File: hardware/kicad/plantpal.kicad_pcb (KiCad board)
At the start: 2 copper layers, 38.4 x 128.5 mm, 117 parts, among them J1 U262-161N-4BVC11, J2 +LIPO, J3 -LIPO, J4 687124182122, Q1 DMG1012UW, Q2 DMG3415U-7, Q3 MMBT3906, Q4 PMV32UP, Q5 DMG1012UW, Q6 AO3407A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

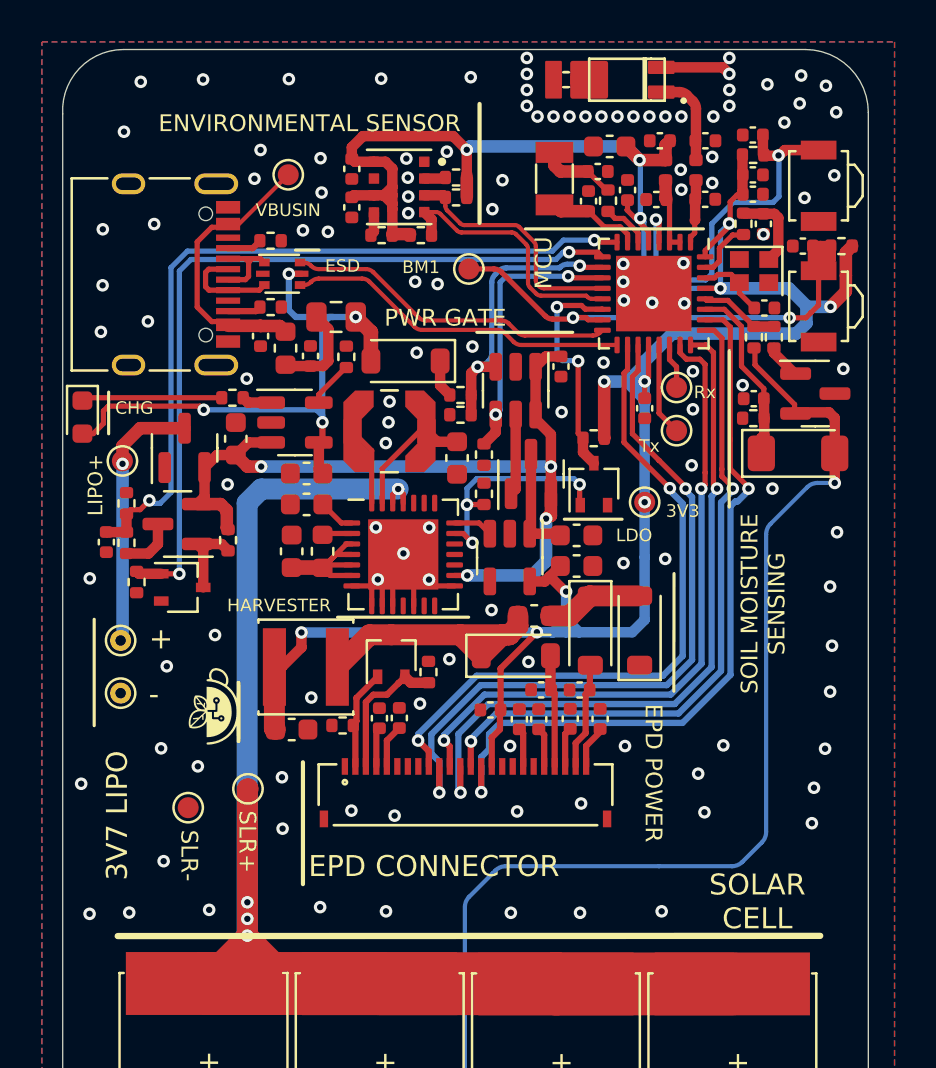
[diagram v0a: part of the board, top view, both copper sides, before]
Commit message: add testpin for chip_enable
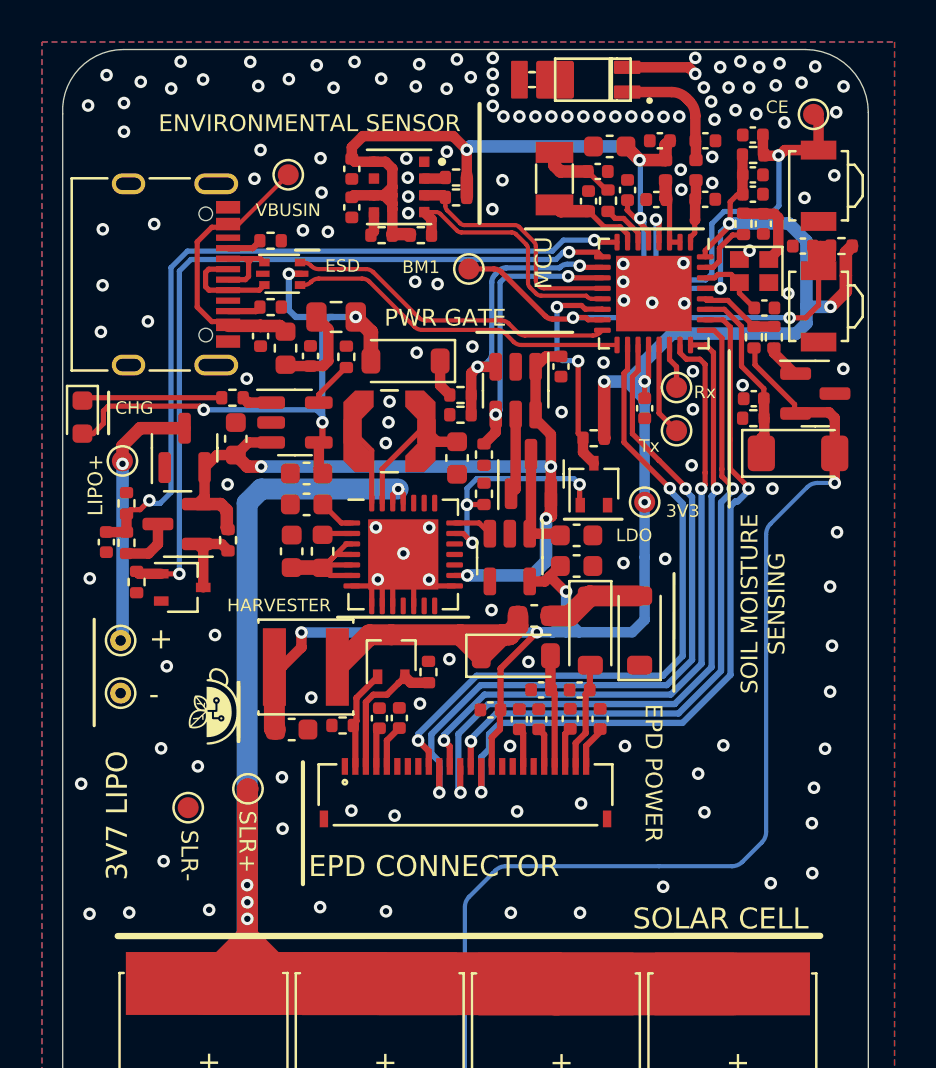
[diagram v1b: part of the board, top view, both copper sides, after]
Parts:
- added TP9: CHIP_EN, TestPoint:TestPoint_Pad_D1.0mm, F.Cu at (126.3, 36.0)
- moved AE1 1.62 mm to (116.0, 34.4)
- moved C12 1.62 mm to (112.8, 34.4)
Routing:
- net +3V3: track 128.0 -> 130.7 mm
- net /Main Controller/CHIP_EN: track 18.4 -> 20.5 mm
- net Net-(AE1-FEED): track 4.52 -> 6.03 mm
- net GND: vias 124 -> 151
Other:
- board text added: "CE"

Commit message: wip
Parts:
- moved TP9 30.3 mm to (124.7, 66.2)
- moved G*** 27.9 mm to (125.0, 70.0), turned to 0 degrees
- moved TP5 12.8 mm to (122.1, 66.7)
- moved C29 1.99 mm to (94.4, 55.8)
- moved R20 1.98 mm to (95.4, 55.8)
- moved Q4 1.86 mm to (97.8, 55.9)
- moved R22 1.83 mm to (100.2, 56.3)
- moved AE1 1.62 mm to (117.6, 34.4)
- moved C12 1.62 mm to (114.5, 34.4)
- moved R23 1.47 mm to (94.9, 57.2), turned to 180 degrees
- moved R21 1.42 mm to (94.9, 54.3), turned to 0 degrees
- moved Q5 0.70 mm to (95.6, 58.9)
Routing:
- net /Main Controller/CHIP_EN: track 20.5 -> 47.6 mm, vias 2 -> 3
- net +3V3: track 130.7 -> 145.6 mm, vias 12 -> 11
- net /Solar Power/SOLAR+: track 70.9 -> 65.5 mm
- net /Main Controller/BATT_MEAS: track 37.1 -> 34.8 mm
- net Net-(AE1-FEED): track 6.03 -> 4.52 mm
- net Net-(Q4-G): track 3.80 -> 5.16 mm
- net /Main Controller/PWR_STATUS: track 11.2 -> 10.1 mm
- net Net-(Q4-D): track 2.64 -> 1.63 mm
- net /Main Controller/BATT_MEAS_EN: track 37.2 -> 36.6 mm
- net +BATT: track 39.1 -> 39.2 mm, vias 4 -> 3
- net Net-(J2-Pin_1): track 12.6 -> 12.8 mm, vias 1 -> 0
- net GND: vias 151 -> 184
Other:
- board text added: "PWR INPUT"

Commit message: wip
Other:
- board text added: "BATT SENSE"

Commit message: wip wake-up button
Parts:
- added Q8: PMV32UP, Package_TO_SOT_SMD:SOT-23, F.Cu at (1.95, 1.73)
- added R27: 5K1, Resistor_SMD:R_0402_1005Metric, F.Cu at (0.95, 4.95)
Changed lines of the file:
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@@
   (net 87 "unconnected-(J4-TSCL-Pad6)")
   (net 88 "unconnected-(J4-TSDA-Pad7)")
+  (net 89 "Net-(Q8-D)")
   (footprint "Capacitor_SMD:C_0402_1005Metric" (layer "F.Cu")
     (at 123.378 39.837)
@@
     (pad "1" thru_hole circle (at 0 0) (size 1 1) (drill 0.5) (layers "*.Cu" "*.Mask")
       (net 43 "Net-(J2-Pin_1)") (pinfunction "Pin_1") (pintype "passive"))
+  )
+  (footprint "Package_TO_SOT_SMD:SOT-23" (layer "F.Cu")
+    (at 1.945 1.725)
+    (descr "SOT, 3 Pin (https://www.jedec.org/system/files/docs/to-236h.pdf variant AB), generated with kicad-footprint-generator ipc_gullwing_generator.py")
+    (tags "SOT TO_SOT_SMD")
+    (property "Distributor" "LCSC")
+    (property "Distributor Link" "https://www.lcsc.com/product-detail/MOSFETs_TECH-PUBLIC-PMV32UP_C2959851.html")
+    (property "Distributor Part Number" "C2959851")
+    (property "Manufacturer" "TECH PUBLIC")
+    (property "Manufacturer Part Number" "PMV32UP")
+    (property "Part Description" "MOSFET P Channel 20V 4A 52mΩ@4.5V")
+    (property "Sheetfile" "power_gate_and_regulator.kicad_sch")
+    (property "Sheetname" "Power Gate and Regulator")
+    (property "ki_description" "P-MOSFET transistor, gate/source/drain")
+    (property "ki_keywords" "transistor PMOS P-MOS P-MOSFET")
+    (attr smd)
+    (fp_text reference "Q8" (at 0 -2.4) (layer "F.SilkS")
+        (effects (font (size 1 1) (thickness 0.15)))
+    )
+    (fp_text value "PMV32UP" (at 0 2.4) (layer "F.Fab")
+        (effects (font (size 1 1) (thickness 0.15)))
+    )
+    (fp_text user "${REFERENCE}" (at 0 0) (layer "F.Fab")
+        (effects (font (size 0.32 0.32) (thickness 0.05)))
+    )
+    (fp_line (start 0 -1.56) (end -1.675 -1.56)
+      (stroke (width 0.12) (type solid)) (layer "F.SilkS"))
+    (fp_line (start 0 -1.56) (end 0.65 -1.56)
+      (stroke (width 0.12) (type solid)) (layer "F.SilkS"))
+    (fp_line (start 0 1.56) (end -0.65 1.56)
+      (stroke (width 0.12) (type solid)) (layer "F.SilkS"))
+    (fp_line (start 0 1.56) (end 0.65 1.56)
+      (stroke (width 0.12) (type solid)) (layer "F.SilkS"))
+    (fp_line (start -1.92 -1.7) (end -1.92 1.7)
+      (stroke (width 0.05) (type solid)) (layer "F.CrtYd"))
+    (fp_line (start -1.92 1.7) (end 1.92 1.7)
+      (stroke (width 0.05) (type solid)) (layer "F.CrtYd"))
+    (fp_line (start 1.92 -1.7) (end -1.92 -1.7)
+      (stroke (width 0.05) (type solid)) (layer "F.CrtYd"))
+    (fp_line (start 1.92 1.7) (end 1.92 -1.7)
+      (stroke (width 0.05) (type solid)) (layer "F.CrtYd"))
+    (fp_line (start -0.65 -1.125) (end -0.325 -1.45)
+      (stroke (width 0.1) (type solid)) (layer "F.Fab"))
+    (fp_line (start -0.65 1.45) (end -0.65 -1.125)
+      (stroke (width 0.1) (type solid)) (layer "F.Fab"))
+    (fp_line (start -0.325 -1.45) (end 0.65 -1.45)
+      (stroke (width 0.1) (type solid)) (layer "F.Fab"))
+    (fp_line (start 0.65 -1.45) (end 0.65 1.45)
+      (stroke (width 0.1) (type solid)) (layer "F.Fab"))
+    (fp_line (start 0.65 1.45) (end -0.65 1.45)
+      (stroke (width 0.1) (type solid)) (layer "F.Fab"))
+    (pad "1" smd roundrect (at -0.9375 -0.95) (size 1.475 0.6) (layers "F.Cu" "F.Paste" "F.Mask") (roundrect_rratio 0.25)
+      (net 11 "/Main Controller/CHIP_EN") (pinfunction "G") (pintype "input"))
+    (pad "2" smd roundrect (at -0.9375 0.95) (size 1.475 0.6) (layers "F.Cu" "F.Paste" "F.Mask") (roundrect_rratio 0.25)
+      (net 16 "+BATT") (pinfunction "S") (pintype "passive"))
+    (pad "3" smd roundrect (at 0.9375 0) (size 1.475 0.6) (layers "F.Cu" "F.Paste" "F.Mask") (roundrect_rratio 0.25)
+      (pinfunction "D") (pintype "passive"))
+    (model "${KICAD6_3DMODEL_DIR}/Package_TO_SOT_SMD.3dshapes/SOT-23.wrl"
+      (offset (xyz 0 0 0))
+      (scale (xyz 1 1 1))
+      (rotate (xyz 0 0 0))
+    )
   )
   (footprint "Capacitor_SMD:C_0402_1005Metric" (layer "F.Cu")
@@
       (offset (xyz 0 0 0))
       (scale (xyz 1 1 1))
+      (rotate (xyz 0 0 0))
+    )
+  )
+  (footprint "Resistor_SMD:R_0402_1005Metric" (layer "F.Cu")
+    (at 0.955 4.945)
+    (descr "Resistor SMD 0402 (1005 Metric), square (rectangular) end terminal, IPC_7351 nominal, (Body size source: IPC-SM-782 page 72, https://www.pcb-3d.com/wordpress/wp-content/uploads/ipc-sm-782a_amendment_1_and_2.pdf), generated with kicad-footprint-generator")
+    (tags "resistor")
+    (property "Distributor" "LCSC")
+    (property "Distributor Link" "https://www.lcsc.com/product-detail/Chip-Resistor-Surface-Mount_UNI-ROYAL-Uniroyal-Elec-0402WGF5101TCE_C25905.html")
+    (property "Distributor Part Number" "C25905")
+    (property "Manufacturer" "UNI-ROYAL(Uniroyal Elec)")
+    (property "Manufacturer Part Number" "0402WGF5101TCE")
+    (property "Part Description" "Resistor 62.5mW ±1% 5.1kΩ")
+    (property "Sheetfile" "power_gate_and_regulator.kicad_sch")
+    (property "Sheetname" "Power Gate and Regulator")
+    (property "ki_description" "Resistor, small symbol")
+    (property "ki_keywords" "R resistor")
+    (attr smd)
+    (fp_text reference "R27" (at 0 -1.17) (layer "F.SilkS")
+        (effects (font (size 1 1) (thickness 0.15)))
+    )
+    (fp_text value "5K1" (at 0 1.17) (layer "F.Fab")
+        (effects (font (size 1 1) (thickness 0.15)))
+    )
+    (fp_text user "${REFERENCE}" (at 0 0) (layer "F.Fab")
+        (effects (font (size 0.26 0.26) (thickness 0.04)))
+    )
+    (fp_line (start -0.153641 -0.38) (end 0.153641 -0.38)
+      (stroke (width 0.12) (type solid)) (layer "F.SilkS"))
+    (fp_line (start -0.153641 0.38) (end 0.153641 0.38)
+      (stroke (width 0.12) (type solid)) (layer "F.SilkS"))
+    (fp_line (start -0.93 -0.47) (end 0.93 -0.47)
+      (stroke (width 0.05) (type solid)) (layer "F.CrtYd"))
+    (fp_line (start -0.93 0.47) (end -0.93 -0.47)
+      (stroke (width 0.05) (type solid)) (layer "F.CrtYd"))
+    (fp_line (start 0.93 -0.47) (end 0.93 0.47)
+      (stroke (width 0.05) (type solid)) (layer "F.CrtYd"))
+    (fp_line (start 0.93 0.47) (end -0.93 0.47)
+      (stroke (width 0.05) (type solid)) (layer "F.CrtYd"))
+    (fp_line (start -0.525 -0.27) (end 0.525 -0.27)
+      (stroke (width 0.1) (type solid)) (layer "F.Fab"))
+    (fp_line (start -0.525 0.27) (end -0.525 -0.27)
+      (stroke (width 0.1) (type solid)) (layer "F.Fab"))
+    (fp_line (start 0.525 -0.27) (end 0.525 0.27)
+      (stroke (width 0.1) (type solid)) (layer "F.Fab"))
+    (fp_line (start 0.525 0.27) (end -0.525 0.27)
+      (stroke (width 0.1) (type solid)) (layer "F.Fab"))
+    (pad "1" smd roundrect (at -0.51 0) (size 0.54 0.64) (layers "F.Cu" "F.Paste" "F.Mask") (roundrect_rratio 0.25)
+      (net 89 "Net-(Q8-D)") (pintype "passive"))
+    (pad "2" smd roundrect (at 0.51 0) (size 0.54 0.64) (layers "F.Cu" "F.Paste" "F.Mask") (roundrect_rratio 0.25)
+      (net 70 "/Main Controller/M_DRV") (pintype "passive"))
+    (model "${KICAD6_3DMODEL_DIR}/Resistor_SMD.3dshapes/R_0402_1005Metric.wrl"
+      (offset (xyz 0 0 0))
+      (scale (xyz 1 1 1))
